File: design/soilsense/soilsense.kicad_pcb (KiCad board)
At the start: 10 copper layers, 70 x 32.5 mm, 25 parts, among them Q1 AO3407, Q2 AO3407, U2 CapSoilSensor_v1.2, U3 ADS1115IDGS, U4 MCP1700x-330xxTO, U5 GXHT30, U6 ESP-01

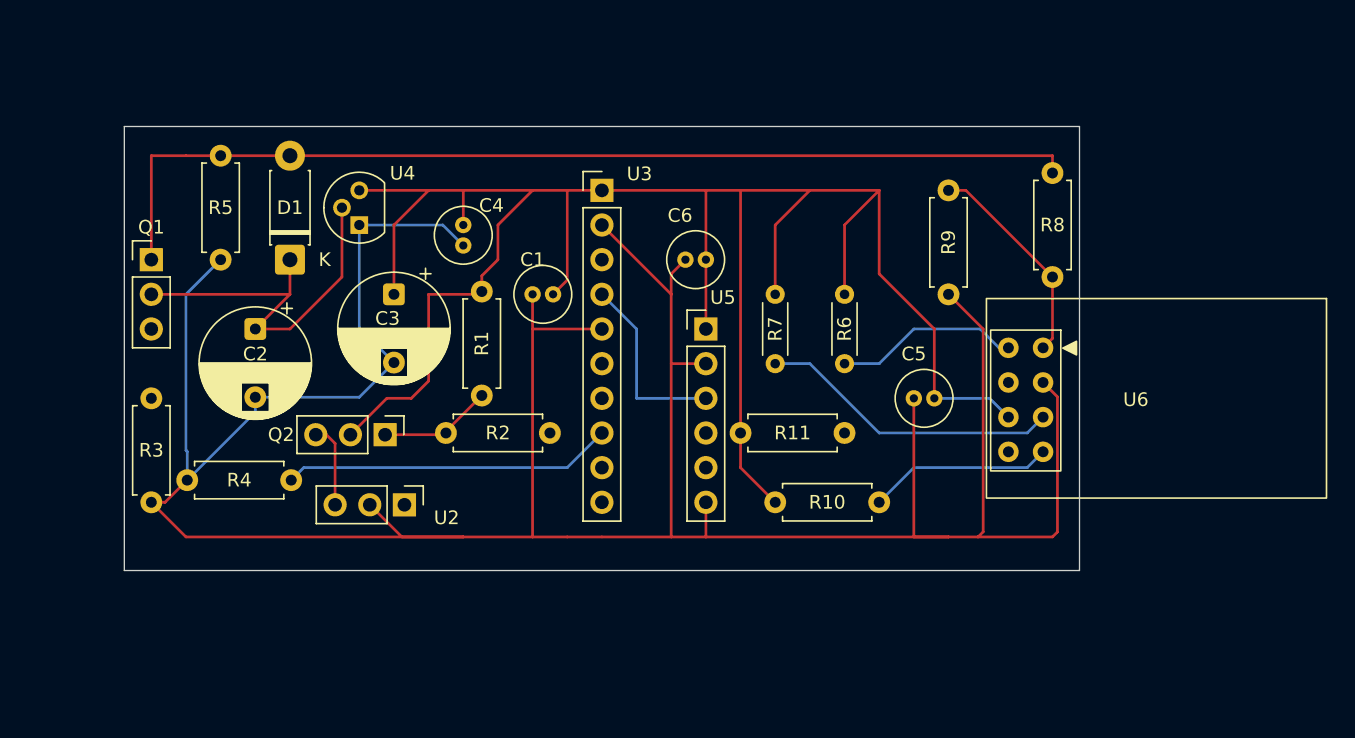
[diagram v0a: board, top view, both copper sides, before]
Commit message: Add enclosure and refine board layout
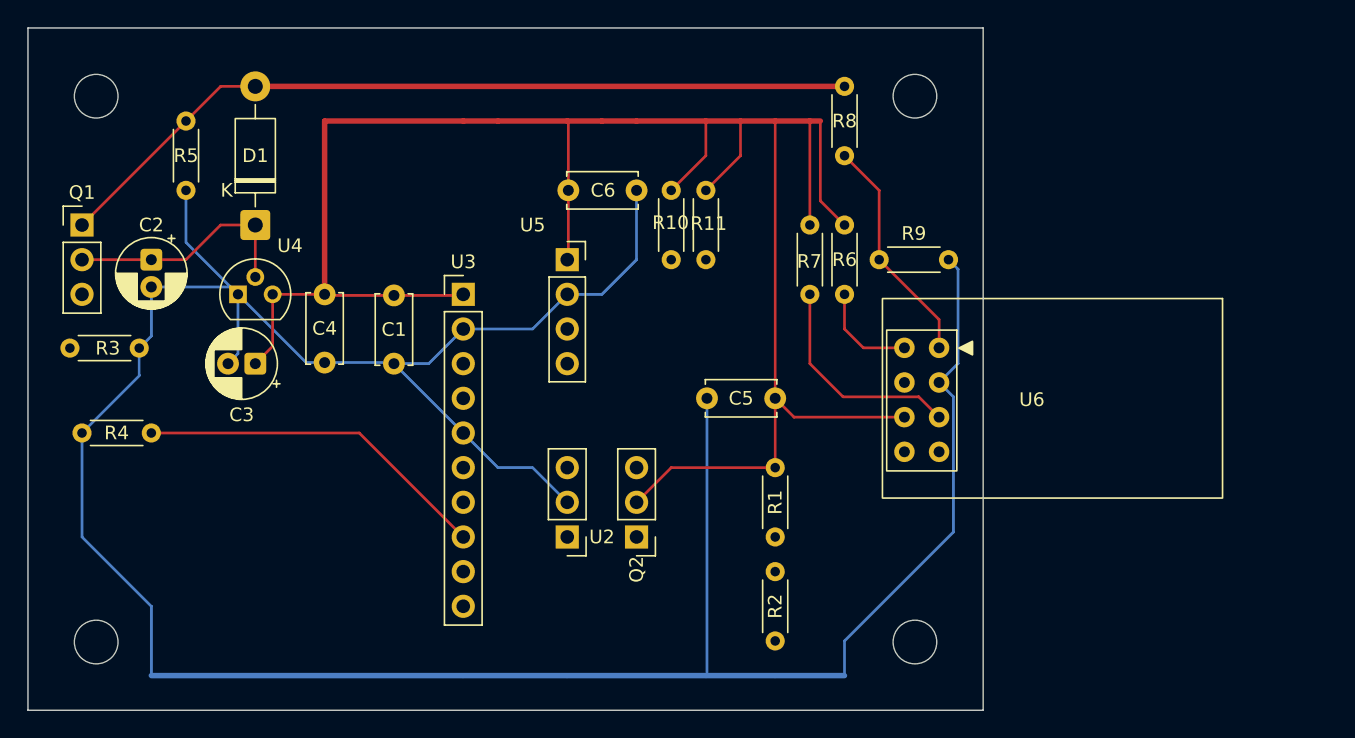
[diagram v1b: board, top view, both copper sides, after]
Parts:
- added REF**: MountingHole_3.2mm_M3, MountingHole:MountingHole_3.2mm_M3, F.Cu at (157.6, 56.6)
- added REF**: MountingHole_3.2mm_M3, MountingHole:MountingHole_3.2mm_M3, F.Cu at (97.6, 56.6)
- added REF**: MountingHole_3.2mm_M3, MountingHole:MountingHole_3.2mm_M3, F.Cu at (157.6, 96.6)
- added REF**: MountingHole_3.2mm_M3, MountingHole:MountingHole_3.2mm_M3, F.Cu at (97.6, 96.6)
- C1, C4, C5, C6: footprint Capacitor_THT:C_Radial_D4.0mm_H5.0mm_P1.50mm -> Capacitor_THT:C_Disc_D5.0mm_W2.5mm_P5.00mm
- C2, C3: footprint Capacitor_THT:CP_Radial_D8.0mm_P5.00mm -> Capacitor_THT:CP_Radial_D5.0mm_P2.00mm
- D1: footprint Diode_THT:D_DO-41_SOD81_P7.62mm_Horizontal -> Diode_THT:D_DO-41_SOD81_P10.16mm_Horizontal
- R1, R10, R11, R2, R3, R4, R5, R8, R9: footprint Resistor_THT:R_Axial_DIN0207_L6.3mm_D2.5mm_P7.62mm_Horizontal -> Resistor_THT:R_Axial_DIN0204_L3.6mm_D1.6mm_P5.08mm_Horizontal
- U5: footprint Connector_PinHeader_2.54mm:PinHeader_1x06_P2.54mm_Vertical -> Connector_PinSocket_2.54mm:PinSocket_1x04_P2.54mm_Vertical
- moved R1 25.1 mm to (147.3, 83.8)
- moved R10 24.1 mm to (139.7, 63.5), turned to -90 degrees
- moved R2 22.5 mm to (147.3, 96.5), turned to 90 degrees
- moved Q2 19.9 mm to (137.2, 88.9), turned to 180 degrees
- moved R11 18.0 mm to (142.2, 63.5), turned to -90 degrees
- moved R8 16.5 mm to (152.4, 55.9)
- moved C5 15.2 mm to (142.3, 78.7)
- moved U3 12.7 mm to (124.5, 71.1)
- moved U2 12.2 mm to (132.1, 88.9), turned to 180 degrees
- moved C1 11.4 mm to (119.4, 76.2), turned to 90 degrees
- moved C3 11.4 mm to (109.2, 76.2), turned to 180 degrees
- moved C4 11.4 mm to (114.3, 71.1)
- moved U5 11.4 mm to (132.1, 68.6)
- moved U4 10.2 mm to (108.0, 71.1), turned to 0 degrees
- moved C2 9.16 mm to (101.6, 68.6)
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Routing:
- net SDA: track 27.3 -> 56.8 mm
- net GND: track 233.7 -> 216.7 mm
- net RX: track 34.2 -> 17.8 mm
- net 5V: track 74.9 -> 60.1 mm
- net Net-(U2-AOUT): track 20.7 -> 8.67 mm
- net Net-(D1-K): track 29.3 -> 17.6 mm
- net SCL: track 31.4 -> 40.5 mm
- net Net-(U6-RST): track 13.6 -> 7.50 mm
- net Net-(U6-CH_PD): track 22.2 -> 16.2 mm
- net Net-(Q2-G): track 8.35 -> 12.7 mm
- net 3.3V: track 158.3 -> 161.7 mm
- net B+: track 24.2 -> 26.0 mm
- net Net-(U6-UTXD): track 15.7 -> 17.0 mm
- net Net-(Q2-D): track 6.18 -> 5.08 mm
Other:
- board size 70 x 32.5 mm -> 70 x 50 mm
